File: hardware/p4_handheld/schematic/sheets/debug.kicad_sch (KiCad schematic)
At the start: 0 parts

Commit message: hw(p4_handheld): audio, storage, debug sheets
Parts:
- added TP1: UART_TX, TestPoint_Pad_D1.5mm, symbol PSP4H:Block2
- added TP2: UART_RX, TestPoint_Pad_D1.5mm, symbol PSP4H:Block2
- added TP3: BOOT, TestPoint_Pad_D1.5mm, symbol PSP4H:Block2
- added TP4: EN, TestPoint_Pad_D1.5mm, symbol PSP4H:Block2
- added TP5: SPARE_GPIO16, TestPoint_Pad_D1.5mm, symbol PSP4H:Block2
- added TP6: SPARE_GPIO17, TestPoint_Pad_D1.5mm, symbol PSP4H:Block2
- added TP7: SPARE_GPIO18, TestPoint_Pad_D1.5mm, symbol PSP4H:Block2
- added TP8: SPARE_GPIO19, TestPoint_Pad_D1.5mm, symbol PSP4H:Block2
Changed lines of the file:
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@@
     (comment 2 "Same-net labels connect; globals cross sheets")
   )
+  (symbol (lib_id "PSP4H:Block2") (at 35 35 0) (unit 1)
+    (exclude_from_sim no) (in_bom yes) (on_board yes) (dnp no) (fields_autoplaced)
+    (property "Reference" "TP1" (at 35 29 0)
+      (effects (font (size 1.27 1.27))))
+    (property "Value" "UART_TX" (at 35 41 0)
+      (effects (font (size 1.27 1.27))))
+    (property "Footprint" "TestPoint_Pad_D1.5mm" (at 35 35 0)
+      (effects (font (size 1.27 1.27)) hide))
+    (property "Datasheet" "~" (at 35 35 0)
+      (effects (font (size 1.27 1.27)) hide))
+    (instances (project "card" (path "/p4_handheld/sheets/debug" (reference "TP1") (unit 1))))
+  )
+  (label "UART_TX" (at 53 30 0) (fields_autoplaced)
+    (effects (font (size 1.27 1.27)) (justify left)))
+  (symbol (lib_id "PSP4H:Block2") (at 80 35 0) (unit 1)
+    (exclude_from_sim no) (in_bom yes) (on_board yes) (dnp no) (fields_autoplaced)
+    (property "Reference" "TP2" (at 80 29 0)
+      (effects (font (size 1.27 1.27))))
+    (property "Value" "UART_RX" (at 80 41 0)
+      (effects (font (size 1.27 1.27))))
+    (property "Footprint" "TestPoint_Pad_D1.5mm" (at 80 35 0)
+      (effects (font (size 1.27 1.27)) hide))
+    (property "Datasheet" "~" (at 80 35 0)
+      (effects (font (size 1.27 1.27)) hide))
+    (instances (project "card" (path "/p4_handheld/sheets/debug" (reference "TP2") (unit 1))))
+  )
+  (label "UART_RX" (at 98 30 0) (fields_autoplaced)
+    (effects (font (size 1.27 1.27)) (justify left)))
+  (symbol (lib_id "PSP4H:Block2") (at 125 35 0) (unit 1)
+    (exclude_from_sim no) (in_bom yes) (on_board yes) (dnp no) (fields_autoplaced)
+    (property "Reference" "TP3" (at 125 29 0)
+      (effects (font (size 1.27 1.27))))
+    (property "Value" "BOOT" (at 125 41 0)
+      (effects (font (size 1.27 1.27))))
+    (property "Footprint" "TestPoint_Pad_D1.5mm" (at 125 35 0)
+      (effects (font (size 1.27 1.27)) hide))
+    (property "Datasheet" "~" (at 125 35 0)
+      (effects (font (size 1.27 1.27)) hide))
+    (instances (project "card" (path "/p4_handheld/sheets/debug" (reference "TP3") (unit 1))))
+  )
+  (label "BOOT" (at 143 30 0) (fields_autoplaced)
+    (effects (font (size 1.27 1.27)) (justify left)))
+  (symbol (lib_id "PSP4H:Block2") (at 170 35 0) (unit 1)
+    (exclude_from_sim no) (in_bom yes) (on_board yes) (dnp no) (fields_autoplaced)
+    (property "Reference" "TP4" (at 170 29 0)
+      (effects (font (size 1.27 1.27))))
+    (property "Value" "EN" (at 170 41 0)
+      (effects (font (size 1.27 1.27))))
+    (property "Footprint" "TestPoint_Pad_D1.5mm" (at 170 35 0)
+      (effects (font (size 1.27 1.27)) hide))
+    (property "Datasheet" "~" (at 170 35 0)
+      (effects (font (size 1.27 1.27)) hide))
+    (instances (project "card" (path "/p4_handheld/sheets/debug" (reference "TP4") (unit 1))))
+  )
+  (label "ESP_EN" (at 188 30 0) (fields_autoplaced)
+    (effects (font (size 1.27 1.27)) (justify left)))
+  (symbol (lib_id "PSP4H:Block2") (at 35 65 0) (unit 1)
+    (exclude_from_sim no) (in_bom yes) (on_board yes) (dnp no) (fields_autoplaced)
+    (property "Reference" "TP5" (at 35 59 0)
+      (effects (font (size 1.27 1.27))))
+    (property "Value" "SPARE_GPIO16" (at 35 71 0)
+      (effects (font (size 1.27 1.27))))
+    (property "Footprint" "TestPoint_Pad_D1.5mm" (at 35 65 0)
+      (effects (font (size 1.27 1.27)) hide))
+    (property "Datasheet" "~" (at 35 65 0)
+      (effects (font (size 1.27 1.27)) hide))
+    (instances (project "card" (path "/p4_handheld/sheets/debug" (reference "TP5") (unit 1))))
+  )
+  (label "SPARE_GPIO16" (at 53 60 0) (fields_autoplaced)
+    (effects (font (size 1.27 1.27)) (justify left)))
+  (symbol (lib_id "PSP4H:Block2") (at 80 65 0) (unit 1)
+    (exclude_from_sim no) (in_bom yes) (on_board yes) (dnp no) (fields_autoplaced)
+    (property "Reference" "TP6" (at 80 59 0)
+      (effects (font (size 1.27 1.27))))
+    (property "Value" "SPARE_GPIO17" (at 80 71 0)
+      (effects (font (size 1.27 1.27))))
+    (property "Footprint" "TestPoint_Pad_D1.5mm" (at 80 65 0)
+      (effects (font (size 1.27 1.27)) hide))
+    (property "Datasheet" "~" (at 80 65 0)
+      (effects (font (size 1.27 1.27)) hide))
+    (instances (project "card" (path "/p4_handheld/sheets/debug" (reference "TP6") (unit 1))))
+  )
+  (label "SPARE_GPIO17" (at 98 60 0) (fields_autoplaced)
+    (effects (font (size 1.27 1.27)) (justify left)))
+  (symbol (lib_id "PSP4H:Block2") (at 125 65 0) (unit 1)
+    (exclude_from_sim no) (in_bom yes) (on_board yes) (dnp no) (fields_autoplaced)
+    (property "Reference" "TP7" (at 125 59 0)
+      (effects (font (size 1.27 1.27))))
+    (property "Value" "SPARE_GPIO18" (at 125 71 0)
+      (effects (font (size 1.27 1.27))))
+    (property "Footprint" "TestPoint_Pad_D1.5mm" (at 125 65 0)
+      (effects (font (size 1.27 1.27)) hide))
+    (property "Datasheet" "~" (at 125 65 0)
+      (effects (font (size 1.27 1.27)) hide))
+    (instances (project "card" (path "/p4_handheld/sheets/debug" (reference "TP7") (unit 1))))
+  )
+  (label "SPARE_GPIO18" (at 143 60 0) (fields_autoplaced)
+    (effects (font (size 1.27 1.27)) (justify left)))
+  (symbol (lib_id "PSP4H:Block2") (at 170 65 0) (unit 1)
+    (exclude_from_sim no) (in_bom yes) (on_board yes) (dnp no) (fields_autoplaced)
+    (property "Reference" "TP8" (at 170 59 0)
+      (effects (font (size 1.27 1.27))))
+    (property "Value" "SPARE_GPIO19" (at 170 71 0)
+      (effects (font (size 1.27 1.27))))
+    (property "Footprint" "TestPoint_Pad_D1.5mm" (at 170 65 0)
+      (effects (font (size 1.27 1.27)) hide))
+    (property "Datasheet" "~" (at 170 65 0)
+      (effects (font (size 1.27 1.27)) hide))
+    (instances (project "card" (path "/p4_handheld/sheets/debug" (reference "TP8") (unit 1))))
+  )
+  (label "SPARE_GPIO19" (at 188 60 0) (fields_autoplaced)
+    (effects (font (size 1.27 1.27)) (justify left)))
+  (global_label "ESP_EN" (shape input) (at 280 20 0) (fields_autoplaced)
+    (effects (font (size 1.27 1.27)) (justify left))
+    (property "Intersheetrefs" "${INTERSHEET_REFS}" (at 280 20 0)
+      (effects (font (size 1.27 1.27)) hide))
+  )
+  (global_label "BOOT" (shape input) (at 280 26 0) (fields_autoplaced)
+    (effects (font (size 1.27 1.27)) (justify left))
+    (property "Intersheetrefs" "${INTERSHEET_REFS}" (at 280 26 0)
+      (effects (font (size 1.27 1.27)) hide))
+  )
+  (global_label "UART_TX" (shape input) (at 280 32 0) (fields_autoplaced)
+    (effects (font (size 1.27 1.27)) (justify left))
+    (property "Intersheetrefs" "${INTERSHEET_REFS}" (at 280 32 0)
+      (effects (font (size 1.27 1.27)) hide))
+  )
+  (global_label "UART_RX" (shape input) (at 280 38 0) (fields_autoplaced)
+    (effects (font (size 1.27 1.27)) (justify left))
+    (property "Intersheetrefs" "${INTERSHEET_REFS}" (at 280 38 0)
+      (effects (font (size 1.27 1.27)) hide))
+  )
+  (global_label "SPARE_GPIO16" (shape input) (at 280 44 0) (fields_autoplaced)
+    (effects (font (size 1.27 1.27)) (justify left))
+    (property "Intersheetrefs" "${INTERSHEET_REFS}" (at 280 44 0)
+      (effects (font (size 1.27 1.27)) hide))
+  )
+  (global_label "SPARE_GPIO17" (shape input) (at 280 50 0) (fields_autoplaced)
+    (effects (font (size 1.27 1.27)) (justify left))
+    (property "Intersheetrefs" "${INTERSHEET_REFS}" (at 280 50 0)
+      (effects (font (size 1.27 1.27)) hide))
+  )
+  (global_label "SPARE_GPIO18" (shape input) (at 280 56 0) (fields_autoplaced)
+    (effects (font (size 1.27 1.27)) (justify left))
+    (property "Intersheetrefs" "${INTERSHEET_REFS}" (at 280 56 0)
+      (effects (font (size 1.27 1.27)) hide))
+  )
+  (global_label "SPARE_GPIO19" (shape input) (at 280 62 0) (fields_autoplaced)
+    (effects (font (size 1.27 1.27)) (justify left))
+    (property "Intersheetrefs" "${INTERSHEET_REFS}" (at 280 62 0)
+      (effects (font (size 1.27 1.27)) hide))
+  )
 )

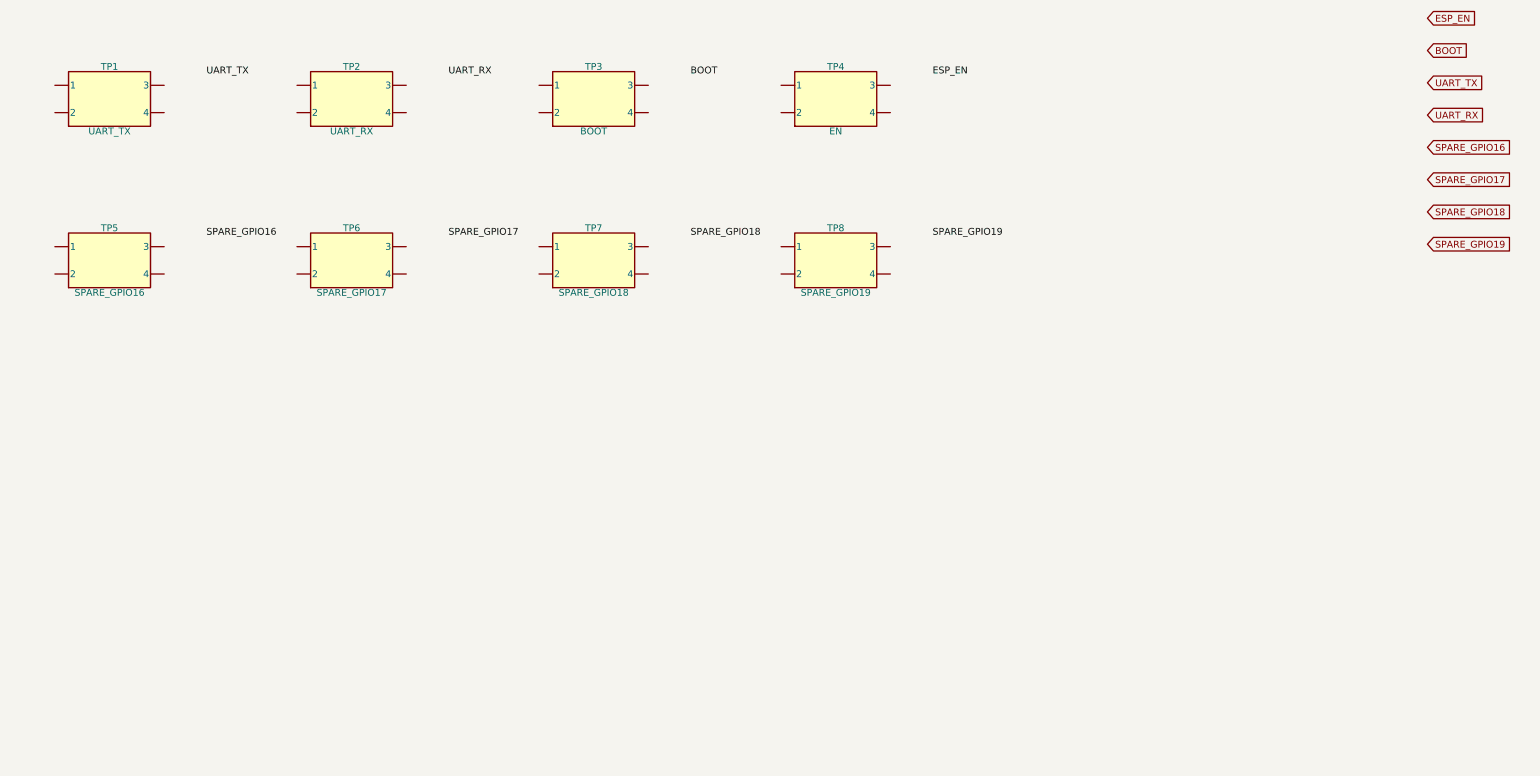
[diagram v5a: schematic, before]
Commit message: hw(p4_handheld): ERC-clean schematic engine (real pins, on-endpoint labels, project symbol lib)
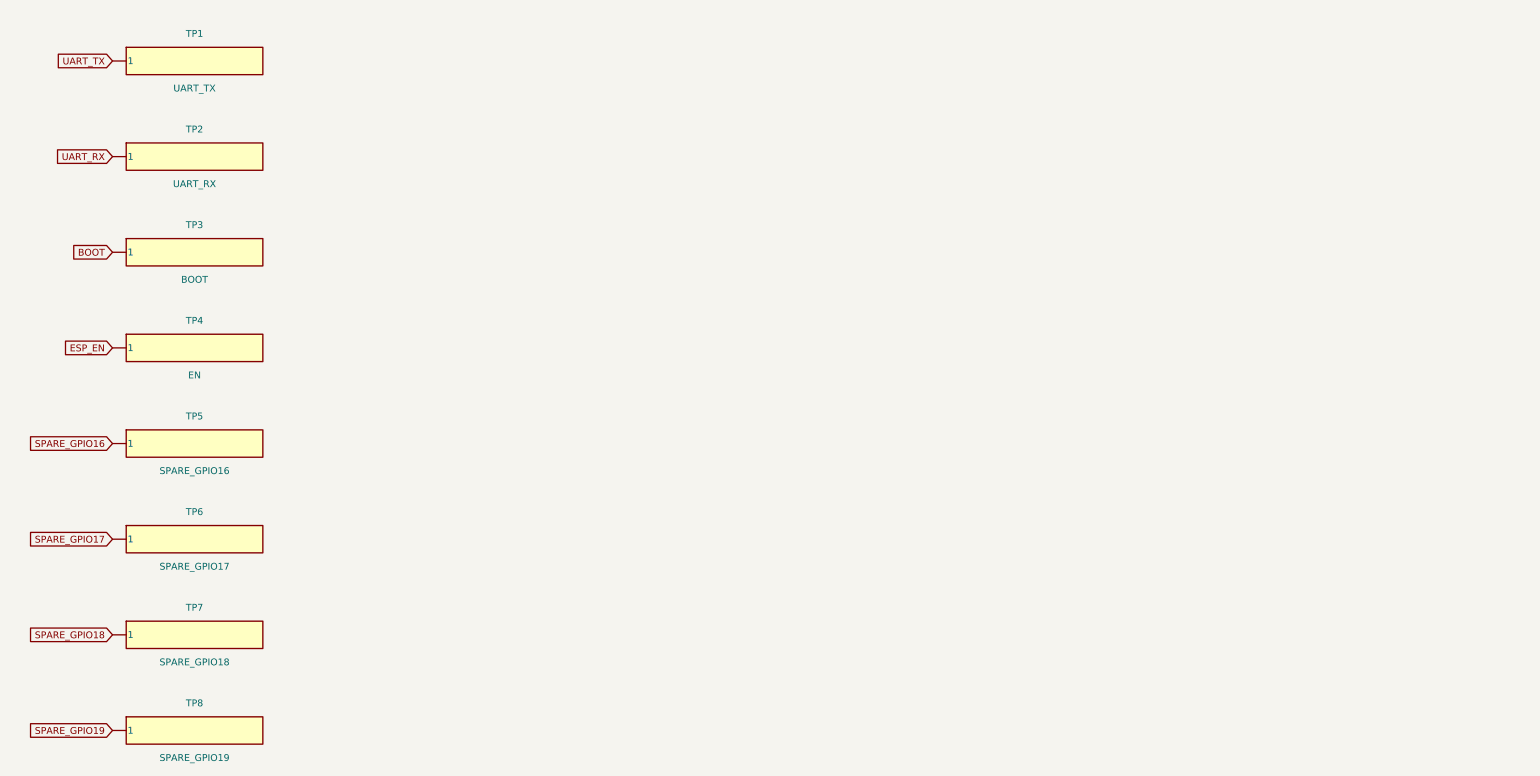
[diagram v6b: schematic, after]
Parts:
- removed TP1: UART_TX, TestPoint_Pad_D1.5mm, symbol PSP4H:Block2
- removed TP2: UART_RX, TestPoint_Pad_D1.5mm, symbol PSP4H:Block2
- removed TP3: BOOT, TestPoint_Pad_D1.5mm, symbol PSP4H:Block2
- removed TP4: EN, TestPoint_Pad_D1.5mm, symbol PSP4H:Block2
- removed TP5: SPARE_GPIO16, TestPoint_Pad_D1.5mm, symbol PSP4H:Block2
- removed TP6: SPARE_GPIO17, TestPoint_Pad_D1.5mm, symbol PSP4H:Block2
- removed TP7: SPARE_GPIO18, TestPoint_Pad_D1.5mm, symbol PSP4H:Block2
- removed TP8: SPARE_GPIO19, TestPoint_Pad_D1.5mm, symbol PSP4H:Block2
- added TP1: UART_TX, symbol PSP4H:SYM_TP1
- added TP2: UART_RX, symbol PSP4H:SYM_TP2
- added TP3: BOOT, symbol PSP4H:SYM_TP3
- added TP4: EN, symbol PSP4H:SYM_TP4
- added TP5: SPARE_GPIO16, symbol PSP4H:SYM_TP5
- added TP6: SPARE_GPIO17, symbol PSP4H:SYM_TP6
- added TP7: SPARE_GPIO18, symbol PSP4H:SYM_TP7
- added TP8: SPARE_GPIO19, symbol PSP4H:SYM_TP8
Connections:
- net BOOT: now also TP3.1
- net ESP_EN: now also TP4.1
- net SPARE_GPIO16: now also TP5.1
- net SPARE_GPIO17: now also TP6.1
- net SPARE_GPIO18: now also TP7.1
- net SPARE_GPIO19: now also TP8.1
- net UART_RX: now also TP2.1
- net UART_TX: now also TP1.1
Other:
- title: PuzzleScript Card — debug -> PuzzleScript P4 Handheld — debug
